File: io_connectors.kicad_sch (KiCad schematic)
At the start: 8 parts, among them J4 OLED Display, J5 E Stop

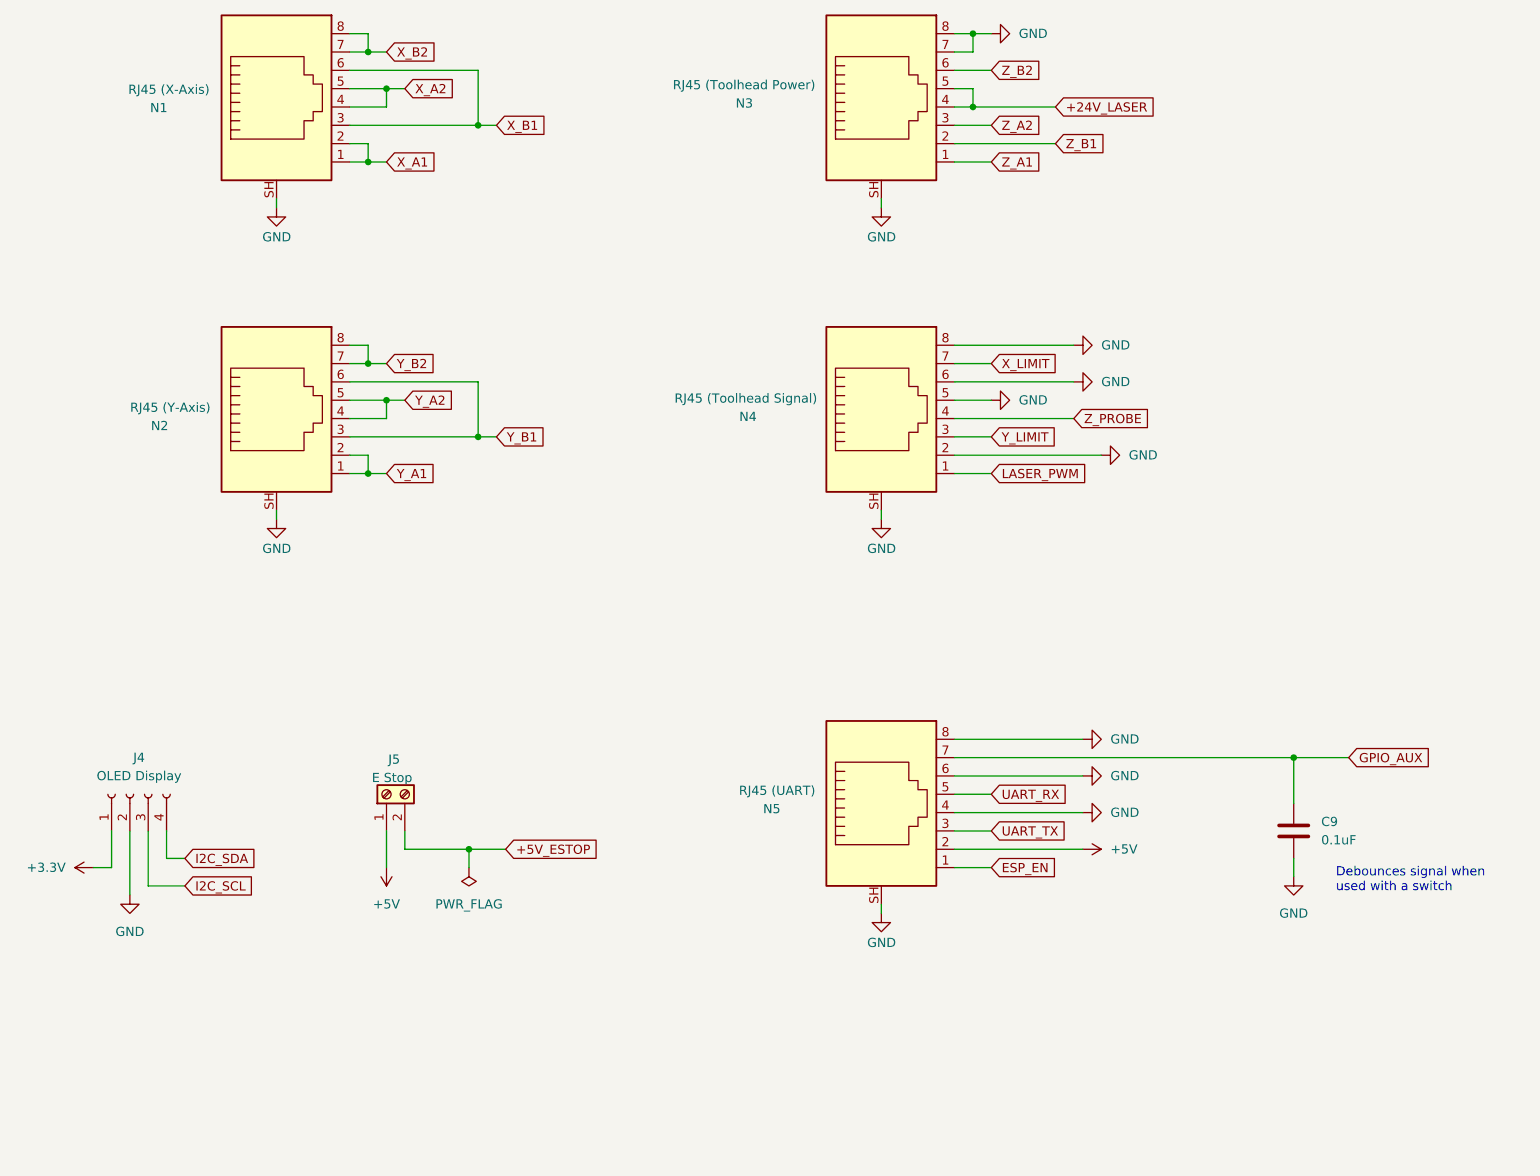
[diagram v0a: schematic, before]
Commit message: rearrange and connect everything
rearrange and connect everything
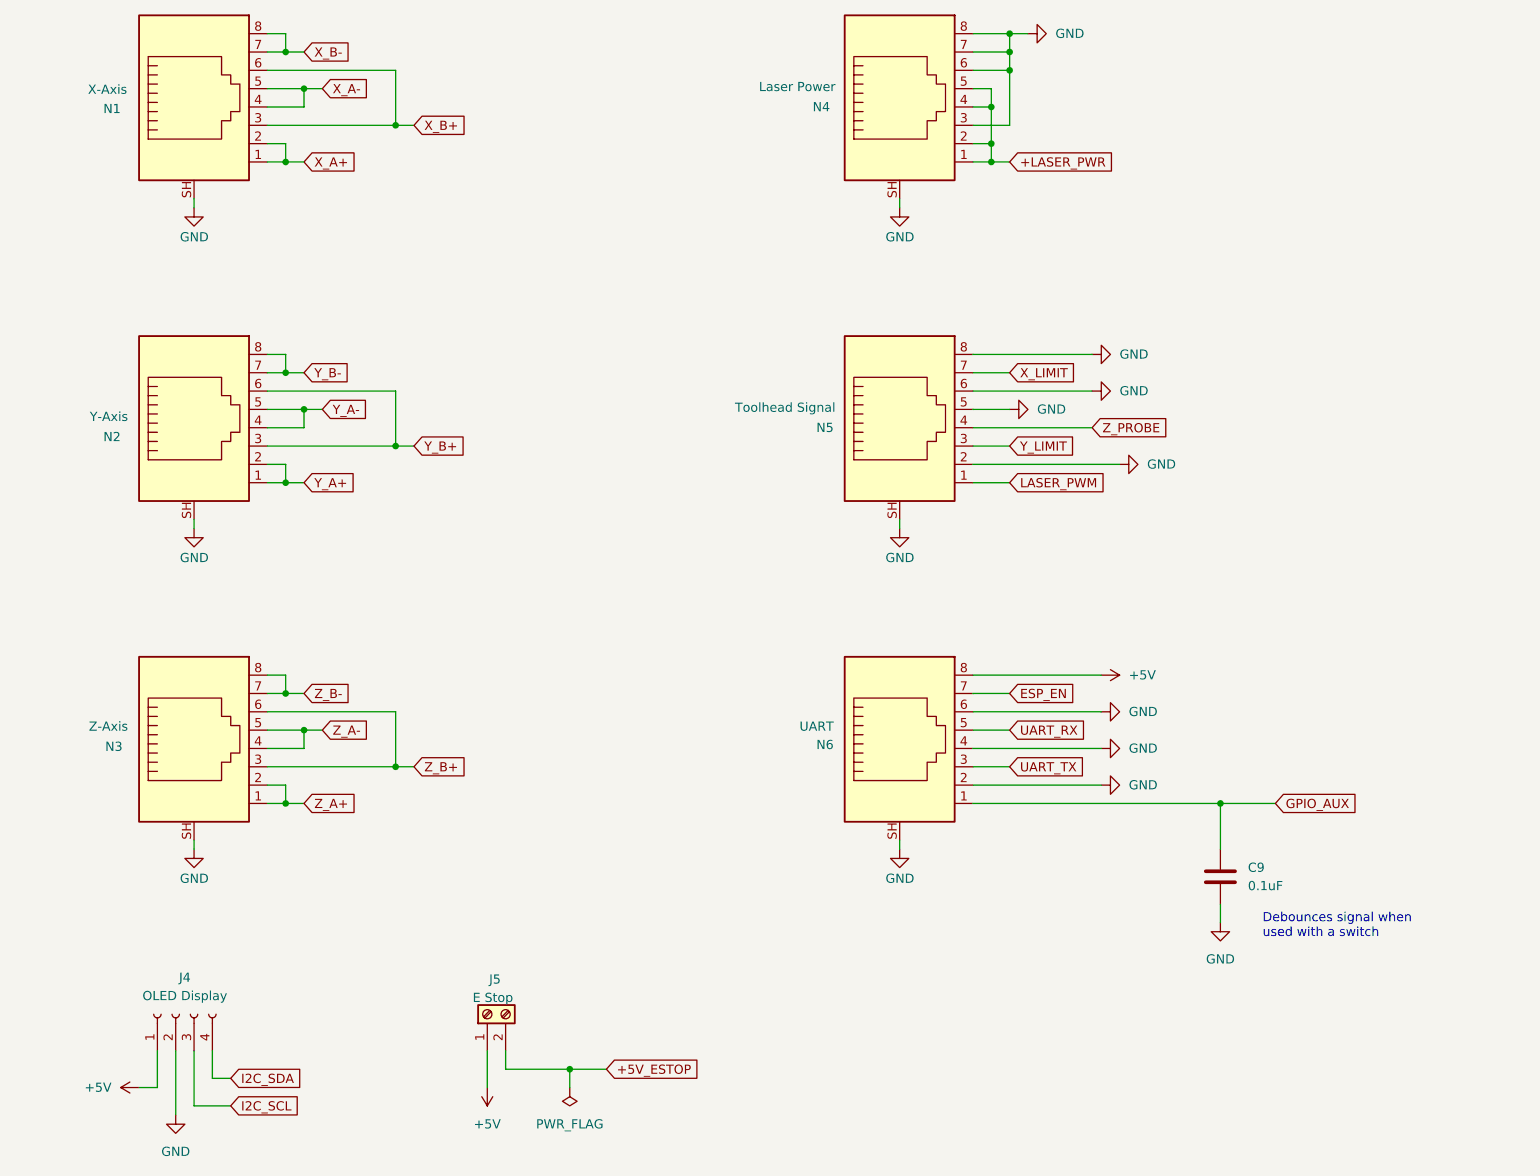
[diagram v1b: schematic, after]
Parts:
- added N5: Toolhead Signal, Connector_RJ:RJ45_HALO_HFJ11-x2450HRL_Horizontal, symbol Connector:RJ45_Shielded
- N1: value RJ45 (X-Axis) -> X-Axis
- N2: value RJ45 (Y-Axis) -> Y-Axis
- N3: value RJ45 (Toolhead Power) -> Z-Axis
- N4: value RJ45 (Toolhead Signal) -> Laser Power
- N6: renamed from N5; value RJ45 (UART) -> UART
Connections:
- net +3.3V is gone; now on net +5V: J4.1 (Pin_1)
- net Z_B1 is gone; now on net Z_A+: N3.2
- net Z_B2 is gone; now on net Z_B+: N3.6
- net +5V: now also N6.8; no longer N6.2
- net ESP_EN: now also N6.7; no longer N6.1
- net GND: now also N4.3, N4.7, N6.2, N5.2, N5.5, N5.6, N5.8, N5.SH; no longer N3.7, N3.8, N4.2, N4.5, N6.8
- net GPIO_AUX: now also N6.1; no longer N6.7
- net LASER_PWM: now also N5.1; no longer N4.1
- net X_LIMIT: now also N5.7; no longer N4.7
- net Y_LIMIT: now also N5.3; no longer N4.3
- net Z_PROBE: now also N5.4; no longer N4.4
- net +24V_LASER renamed Z_A-
- net X_A1 renamed X_A+
- net X_A2 renamed X_A-
- net X_B1 renamed X_B+
- net X_B2 renamed X_B-
- net Y_A1 renamed Y_A+
- net Y_A2 renamed Y_A-
- net Y_B1 renamed Y_B+
- net Y_B2 renamed Y_B-
- net Z_A1 renamed Z_A+
- net Z_A2 renamed Z_B+
- new net +LASER_PWR: N4.1, N4.2, N4.4, N4.5
- new net Z_B-: N3.7, N3.8
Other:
- moved on the sheet: C9, J4, J5, N1, N2, N3, N4, N6
